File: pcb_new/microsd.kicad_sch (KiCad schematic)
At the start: 27 parts, among them J5 DM3AT-SF-PEJM5(40), J6 FFC2B35-10-T, U3 TS3DV416DGGR

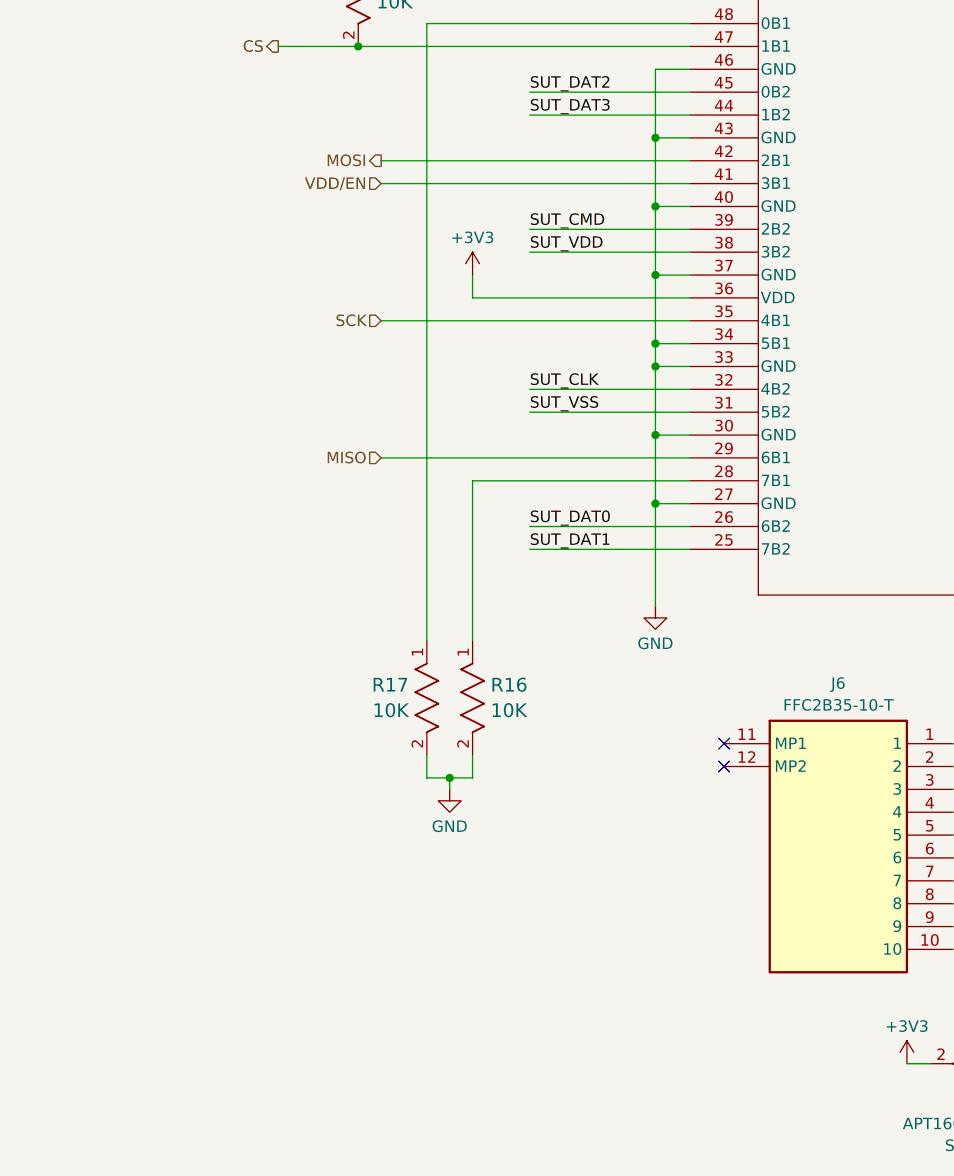
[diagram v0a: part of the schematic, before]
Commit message: put sdcard vcc on switch instead of source from gpio (ref #97)
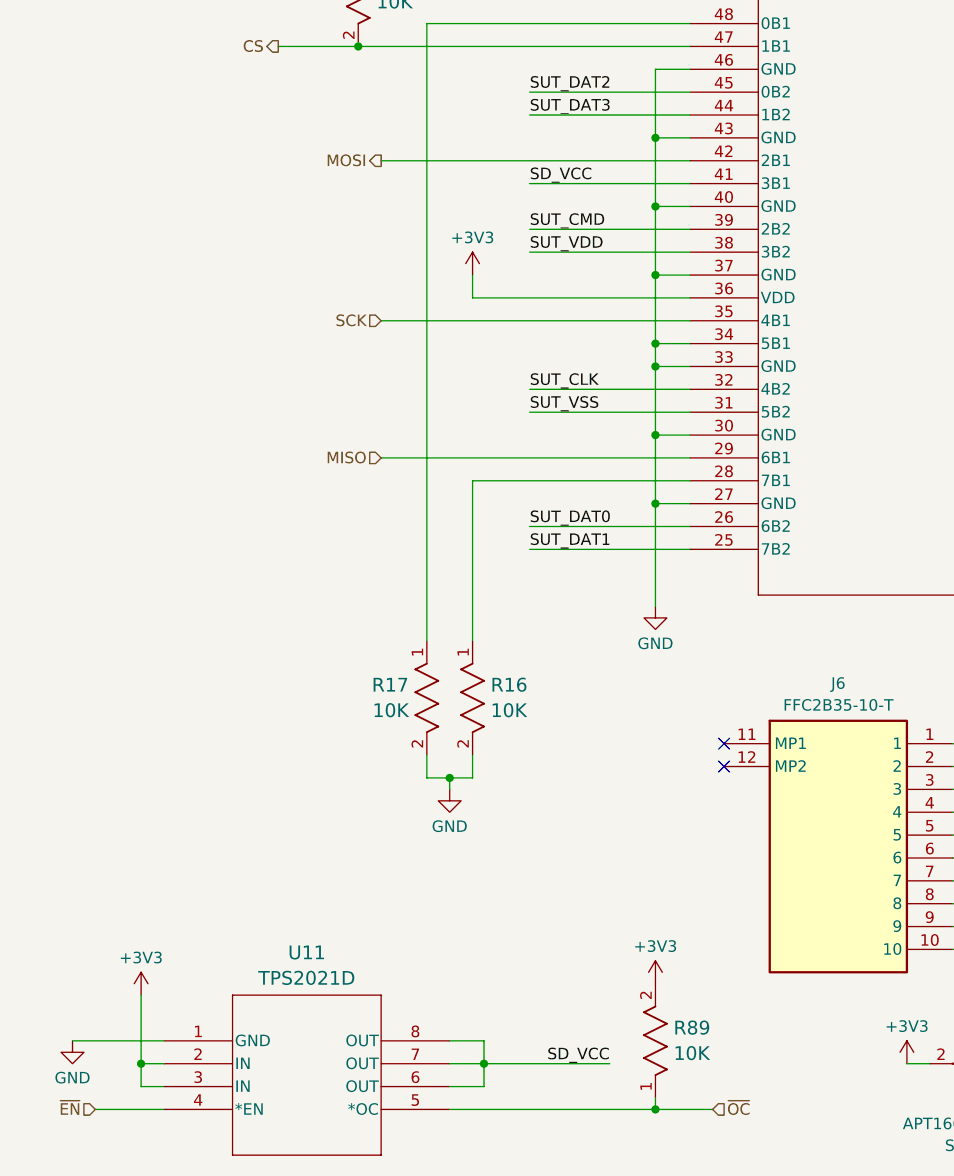
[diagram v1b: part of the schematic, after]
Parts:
- added R89: 10K, OroLink:STA_RMCF0402_STP, symbol OroLink:RMCF0402FT10K0
- added U11: TPS2021D, OroLink:D8, symbol OroLink:TPS2021D
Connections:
- net +3V3: now also R89.2, U11.2 (IN), U11.3 (IN)
- net GND: now also U11.1 (GND)
- net VDD/EN renamed SD_VCC
- net SD_VCC: now also U11.6 (OUT), U11.7 (OUT), U11.8 (OUT)
- new net ~{EN}: U11.4 (*EN)
- new net ~{OC}: R89.1, U11.5 (*OC)

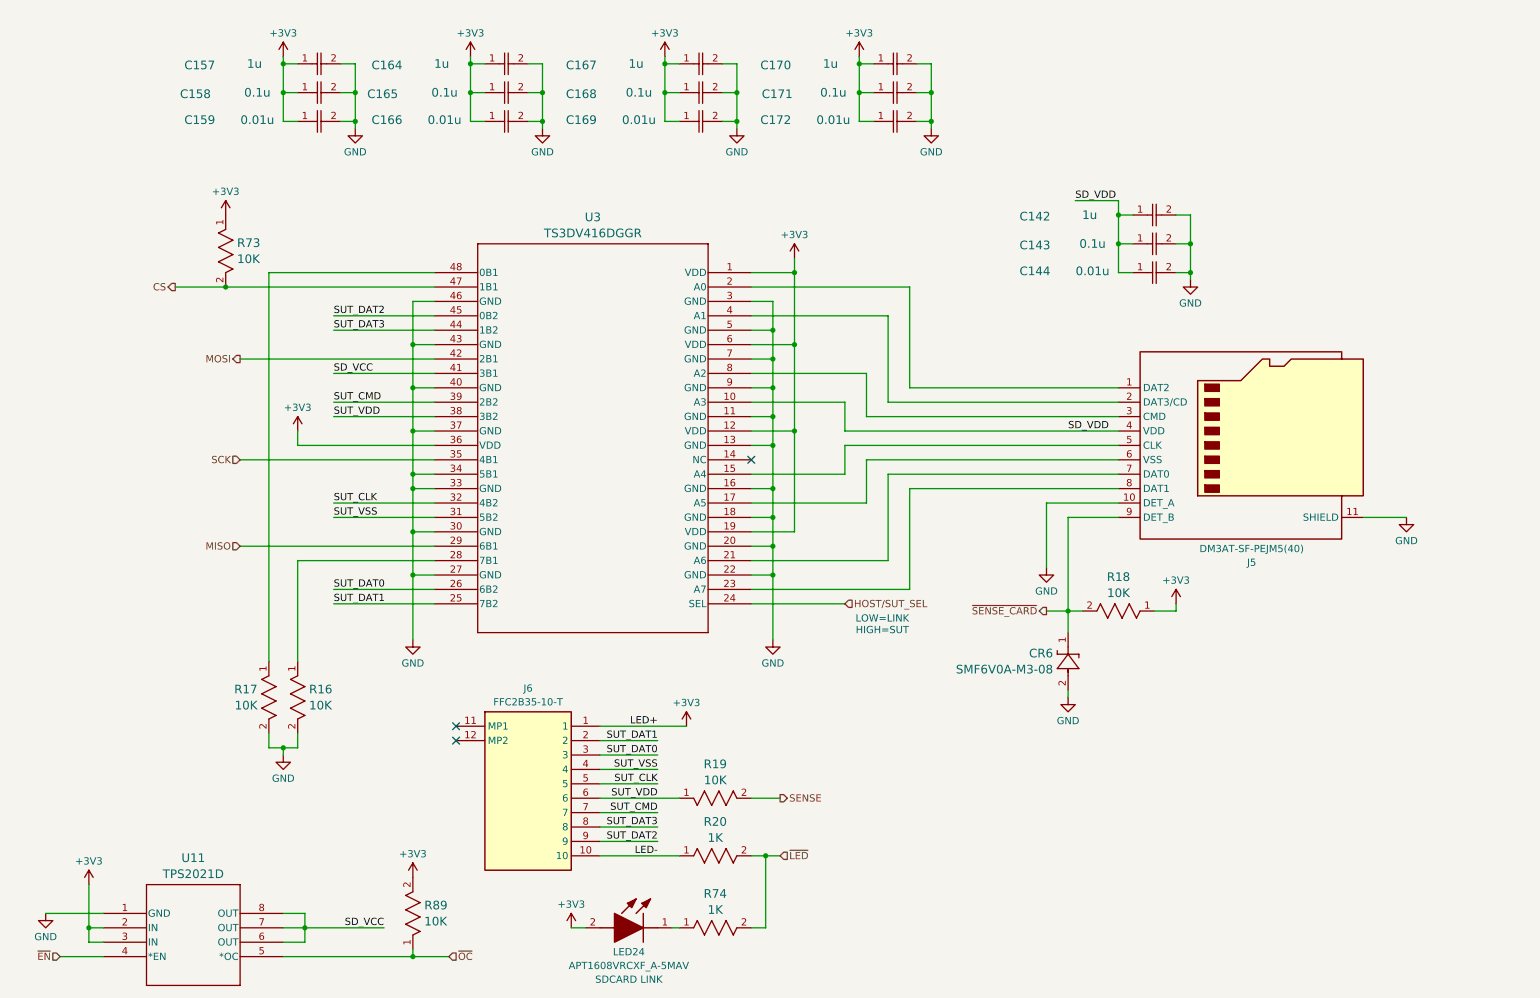
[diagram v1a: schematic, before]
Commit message: replace microsd slot (ref #95) and triangulate debug leds
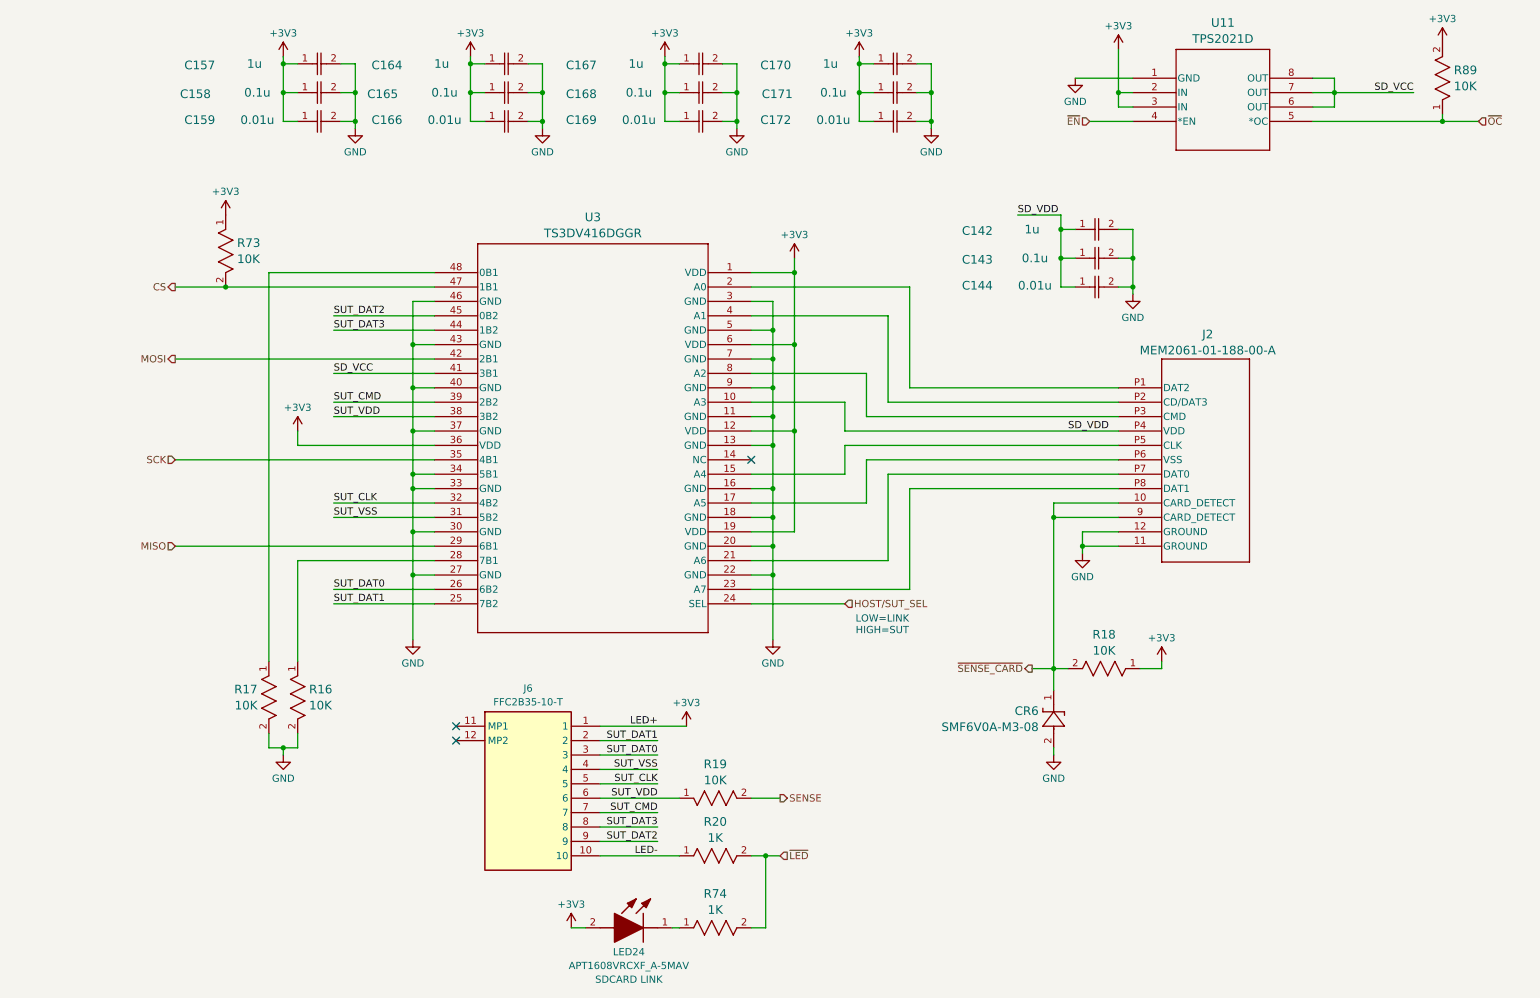
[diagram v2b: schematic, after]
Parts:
- removed J5: DM3AT-SF-PEJM5(40), OroLink:microSD_HC_Hirose_DM3AT-SF-PEJM5-FIXED, symbol OroLink:DM3AT-SF-PEJM5(40)
- added J2: MEM2061-01-188-00-A, OroLink:MEM2061-01-188-00-A_GCT, symbol OroLink:MEM2061-01-188-00-A
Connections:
- net GND: now also J2.11 (GROUND), J2.12 (GROUND)
- net SD_VDD: now also J2.P4 (VDD)
- net ~{SENSE_CARD}: now also J2.10 (CARD_DETECT), J2.9 (CARD_DETECT)
- net at U3.2 (A0): now also J2.P1 (DAT2)
- net at U3.4 (A1): now also J2.P2 (CD/DAT3)
- net at U3.8 (A2): now also J2.P3 (CMD)
- net at U3.15 (A4): now also J2.P5 (CLK)
- net at U3.17 (A5): now also J2.P6 (VSS)
- net at U3.21 (A6): now also J2.P7 (DAT0)
- net at U3.23 (A7): now also J2.P8 (DAT1)
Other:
- moved on the sheet: C142, C143, C144, CR6, R18, R89, U11
